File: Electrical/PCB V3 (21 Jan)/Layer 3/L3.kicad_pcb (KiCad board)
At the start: 2 copper layers, 129.9 x 110 mm, 28 parts, among them J1 Conn_01x06, J2 Conn_02x04_Odd_Even, J3 Conn_01x06, J4 Conn_01x06, J5 Conn_01x06, U2 113991054, U3 4754

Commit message: deleted some l3 stuff to clear up folders, open and closed l3
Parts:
- J2: value Conn_02x04_Odd_Even -> Conn_02x08_Odd_Even
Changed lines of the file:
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@@
 			)
 		)
-		(property "Value" "Conn_02x04_Odd_Even"
+		(property "Value" "Conn_02x08_Odd_Even"
 			(at 8.75 -3.4 90)
 			(layer "B.Fab")

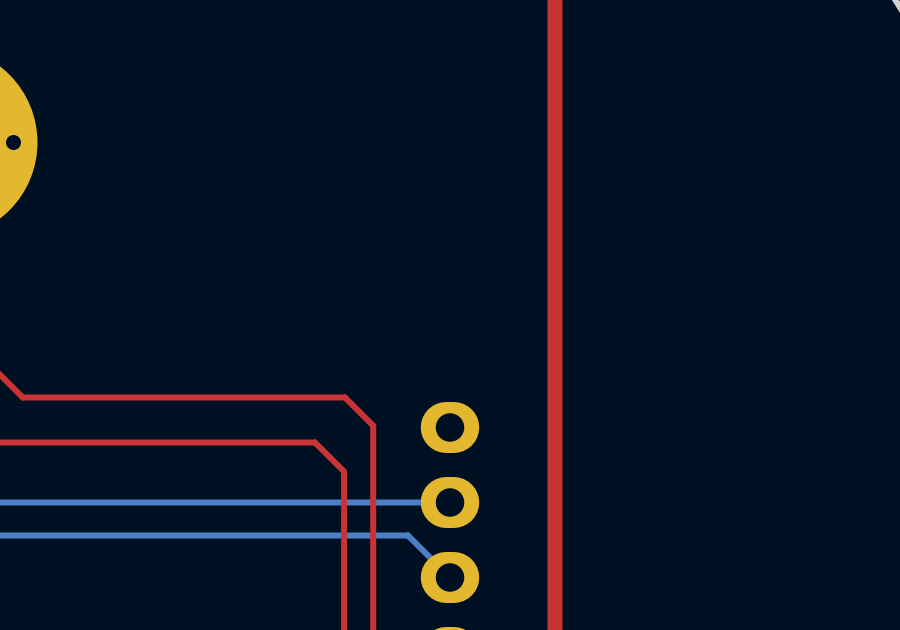
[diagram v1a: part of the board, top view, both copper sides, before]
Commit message: fixed l2 caps positon, export new l2 step. fixed l3 jst from eh to xh, realised need to flip l2 jst
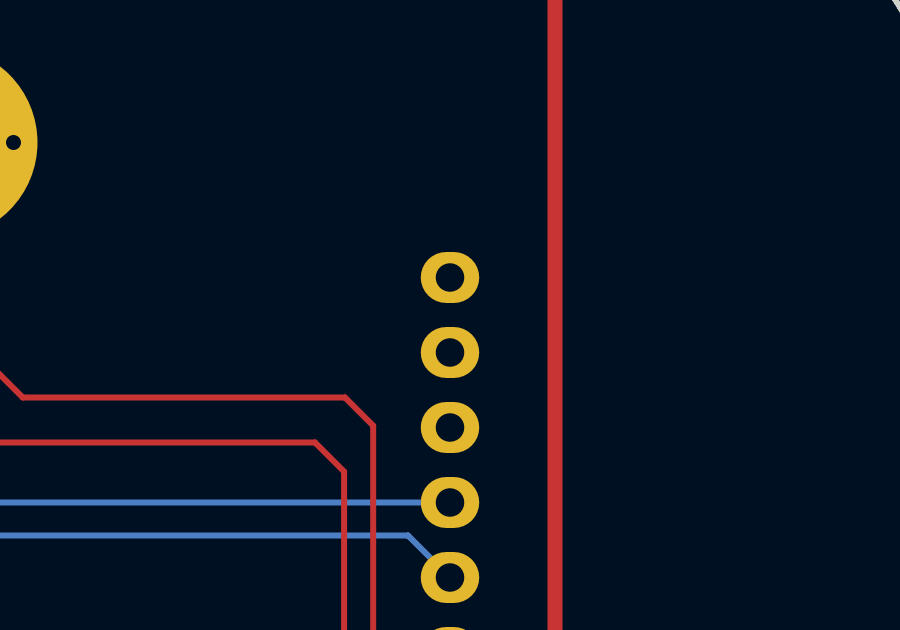
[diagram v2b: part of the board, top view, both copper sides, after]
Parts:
- J2: footprint Connector_JST:JST_EH_B8B-EH-A_1x08_P2.50mm_Vertical -> Connector_JST:JST_XH_B10B-XH-A_1x10_P2.50mm_Vertical
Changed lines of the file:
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@@
 			(at 0 15.03 0)
 			(layer "F.Fab")
+			(hide yes)
 			(effects
 				(font
@@
 			(at 0 15.03 90)
 			(layer "F.Fab")
+			(hide yes)
 			(effects
 				(font
@@
 			(at 0 15.03 90)
 			(layer "F.Fab")
+			(hide yes)
 			(effects
 				(font
@@
 		)
 		(property "Value" "Conn_01x06"
-			(at 0 15.03 0)
+			(at -0.75 -2.400001 0)
 			(layer "F.Fab")
+			(hide yes)
 			(effects
 				(font
@@
 		)
 	)
-	(footprint "Connector_JST:JST_EH_B8B-EH-A_1x08_P2.50mm_Vertical"
+	(footprint "Connector_JST:JST_XH_B10B-XH-A_1x10_P2.50mm_Vertical"
 		(layer "B.Cu")
 		(at 253.740001 84.530001 90)
-		(descr "JST EH series connector, B8B-EH-A (http://www.jst-mfg.com/product/pdf/eng/eEH.pdf), generated with kicad-footprint-generator")
-		(tags "connector JST EH vertical")
+		(descr "JST XH series connector, B10B-XH-A (http://www.jst-mfg.com/product/pdf/eng/eXH.pdf), generated with kicad-footprint-generator")
+		(tags "connector JST XH side entry")
 		(property "Reference" "J2"
-			(at 8.75 2.8 90)
+			(at 11.25 3.55 -90)
 			(layer "B.SilkS")
-			(hide yes)
 			(effects
 				(font
@@
 		)
 		(property "Value" "Conn_02x08_Odd_Even"
-			(at 8.75 -3.4 90)
+			(at 11.25 -4.6 -90)
 			(layer "B.Fab")
-			(hide yes)
 			(effects
 				(font
@@
 			)
 		)
-		(property "Footprint" "Connector_JST:JST_EH_B8B-EH-A_1x08_P2.50mm_Vertical"
+		(property "Footprint" "Connector_JST:JST_XH_B10B-XH-A_1x10_P2.50mm_Vertical"
 			(at 0 0 -90)
 			(unlocked yes)
@@
 		(attr through_hole)
 		(fp_line
-			(start -0.41 -2.61)
-			(end -2.91 -2.61)
+			(start 25.06 -3.51)
+			(end -2.56 -3.51)
+			(stroke
+				(width 0.12)
+				(type solid)
+			)
+			(layer "B.SilkS")
+		)
+		(fp_line
+			(start -2.56 -3.51)
+			(end -2.56 2.46)
+			(stroke
+				(width 0.12)
+				(type solid)
+			)
+			(layer "B.SilkS")
+		)
+		(fp_line
+			(start 24.3 -2.75)
+			(end 24.3 0.2)
+			(stroke
+				(width 0.12)
+				(type solid)
+			)
+			(layer "B.SilkS")
+		)
+		(fp_line
+			(start 11.25 -2.75)
+			(end 24.3 -2.75)
+			(stroke
+				(width 0.12)
+				(type solid)
+			)
+			(layer "B.SilkS")
+		)
+		(fp_line
+			(start 11.25 -2.75)
+			(end -1.8 -2.75)
+			(stroke
+				(width 0.12)
+				(type solid)
+			)
+			(layer "B.SilkS")
+		)
+		(fp_line
+			(start -1.8 -2.75)
+			(end -1.8 0.2)
+			(stroke
+				(width 0.12)
+				(type solid)
+			)
+			(layer "B.SilkS")
+		)
+		(fp_line
+			(start 24.3 0.2)
+			(end 25.05 0.2)
+			(stroke
+				(width 0.12)
+				(type solid)
+			)
+			(layer "B.SilkS")
+		)
+		(fp_line
+			(start -1.8 0.2)
+			(end -2.55 0.2)
 			(stroke
 				(width 0.12)
@@
 		)
 		(fp_line
-			(start -2.91 -2.61)
-			(end -2.91 -0.11)
+			(start -2.85 1.5)
+			(end -2.85 2.75)
 			(stroke
 				(width 0.12)
@@
 		)
 		(fp_line
-			(start 20.11 -2.31)
-			(end -2.61 -2.31)
+			(start 25.05 1.7)
+			(end 23.25 1.7)
 			(stroke
 				(width 0.12)
@@
 		)
 		(fp_line
-			(start 19.11 -2.31)
-			(end 19.11 -0.81)
+			(start 23.25 1.7)
+			(end 23.25 2.45)
 			(stroke
 				(width 0.12)
@@
 		)
 		(fp_line
-			(start -1.61 -2.31)
-			(end -1.61 -0.81)
+			(start 21.75 1.7)
+			(end 0.75 1.7)
 			(stroke
 				(width 0.12)
@@
 		)
 		(fp_line
-			(start -2.61 -2.31)
-			(end -2.61 1.71)
+			(start 0.75 1.7)
+			(end 0.75 2.45)
 			(stroke
 				(width 0.12)
@@
 		)
 		(fp_line
-			(start 19.11 -0.81)
-			(end 20.11 -0.81)
+			(start -0.75 1.7)
+			(end -2.55 1.7)
 			(stroke
 				(width 0.12)
@@
 		)
 		(fp_line
-			(start -1.61 -0.81)
-			(end -2.61 -0.81)
+			(start -2.55 1.7)
+			(end -2.55 2.45)
 			(stroke
 				(width 0.12)
@@
 		)
 		(fp_line
-			(start 20.11 0)
-			(end 19.61 0)
+			(start 25.05 2.45)
+			(end 25.05 1.7)
 			(stroke
 				(width 0.12)
@@
 		)
 		(fp_line
-			(start 19.61 0)
-			(end 19.61 1.21)
+			(start 23.25 2.45)
+			(end 25.05 2.45)
 			(stroke
 				(width 0.12)
@@
 		)
 		(fp_line
-			(start -2.11 0)
-			(end -2.61 0)
+			(start 21.75 2.45)
+			(end 21.75 1.7)
 			(stroke
 				(width 0.12)
@@
 		)
 		(fp_line
-			(start 19.61 1.21)
-			(end -2.11 1.21)
+			(start 0.75 2.45)
+			(end 21.75 2.45)
 			(stroke
 				(width 0.12)
@@
 		)
 		(fp_line
-			(start -2.11 1.21)
-			(end -2.11 0)
+			(start -0.75 2.45)
+			(end -0.75 1.7)
 			(stroke
 				(width 0.12)
@@
 		)
 		(fp_line
-			(start 20.11 1.71)
-			(end 20.11 -2.31)
+			(start -2.55 2.45)
+			(end -0.75 2.45)
 			(stroke
 				(width 0.12)
@@
 		)
 		(fp_line
-			(start -2.61 1.71)
-			(end 20.11 1.71)
+			(start 25.06 2.46)
+			(end 25.06 -3.51)
 			(stroke
 				(width 0.12)
@@
 		)
 		(fp_line
-			(start 20.5 -2.7)
-			(end -3 -2.7)
+			(start -2.56 2.46)
+			(end 25.06 2.46)
+			(stroke
+				(width 0.12)
+				(type solid)
+			)
+			(layer "B.SilkS")
+		)
+		(fp_line
+			(start -2.85 2.75)
+			(end -1.6 2.75)
+			(stroke
+				(width 0.12)
+				(type solid)
+			)
+			(layer "B.SilkS")
+		)
+		(fp_line
+			(start 25.45 -3.9)
+			(end -2.95 -3.9)
 			(stroke
 				(width 0.05)
@@
 		)
 		(fp_line
-			(start -3 -2.7)
-			(end -3 2.1)
+			(start -2.95 -3.9)
+			(end -2.95 2.85)
 			(stroke
 				(width 0.05)
@@
 		)
 		(fp_line
-			(start 20.5 2.1)
-			(end 20.5 -2.7)
+			(start 25.45 2.85)
+			(end 25.45 -3.9)
 			(stroke
 				(width 0.05)
@@
 		)
 		(fp_line
-			(start -3 2.1)
-			(end 20.5 2.1)
+			(start -2.95 2.85)
+			(end 25.45 2.85)
 			(stroke
 				(width 0.05)
@@
 		)
 		(fp_line
-			(start -0.41 -2.61)
-			(end -2.91 -2.61)
+			(start 24.95 -3.4)
+			(end -2.45 -3.4)
 			(stroke
 				(width 0.1)
@@
 		)
 		(fp_line
-			(start -2.91 -2.61)
-			(end -2.91 -0.11)
+			(start -2.45 -3.4)
+			(end -2.45 2.35)
 			(stroke
 				(width 0.1)
@@
 		)
 		(fp_line
-			(start 20 -2.2)
-			(end -2.5 -2.2)
+			(start 0 1.35)
+			(end -0.625 2.35)
 			(stroke
 				(width 0.1)
@@
 		)
 		(fp_line
-			(start -2.5 -2.2)
-			(end -2.5 1.6)
+			(start 24.95 2.35)
+			(end 24.95 -3.4)
 			(stroke
 				(width 0.1)
@@
 		)
 		(fp_line
-			(start 20 1.6)
-			(end 20 -2.2)
+			(start 0.625 2.35)
+			(end 0 1.35)
 			(stroke
 				(width 0.1)
@@
 		)
 		(fp_line
-			(start -2.5 1.6)
-			(end 20 1.6)
+			(start -2.45 2.35)
+			(end 24.95 2.35)
 			(stroke
 				(width 0.1)
@@
 			(layer "B.Fab")
 		)
+		(fp_text user "${REFERENCE}"
+			(at 11.25 -2.7 -90)
+			(layer "B.Fab")
+			(effects
+				(font
+					(size 1 1)
+					(thickness 0.15)
+				)
+				(justify mirror)
+			)
+		)
 		(pad "1" thru_hole roundrect
 			(at 0 0 90)
@@
 			(pintype "passive")
 		)
-		(model "${KICAD8_3DMODEL_DIR}/Connector_JST.3dshapes/JST_EH_B8B-EH-A_1x08_P2.50mm_Vertical.wrl"
+		(pad "9" thru_hole oval
+			(at 20 0 90)
+			(size 1.7 1.95)
+			(drill 0.95)
+			(layers "*.Cu" "*.Mask")
+			(remove_unused_layers no)
+		)
+		(pad "10" thru_hole oval
+			(at 22.5 0 90)
+			(size 1.7 1.95)
+			(drill 0.95)
+			(layers "*.Cu" "*.Mask")
+			(remove_unused_layers no)
+		)
+		(model "${KICAD8_3DMODEL_DIR}/Connector_JST.3dshapes/JST_XH_B10B-XH-A_1x10_P2.50mm_Vertical.wrl"
 			(offset
 				(xyz 0 0 0)

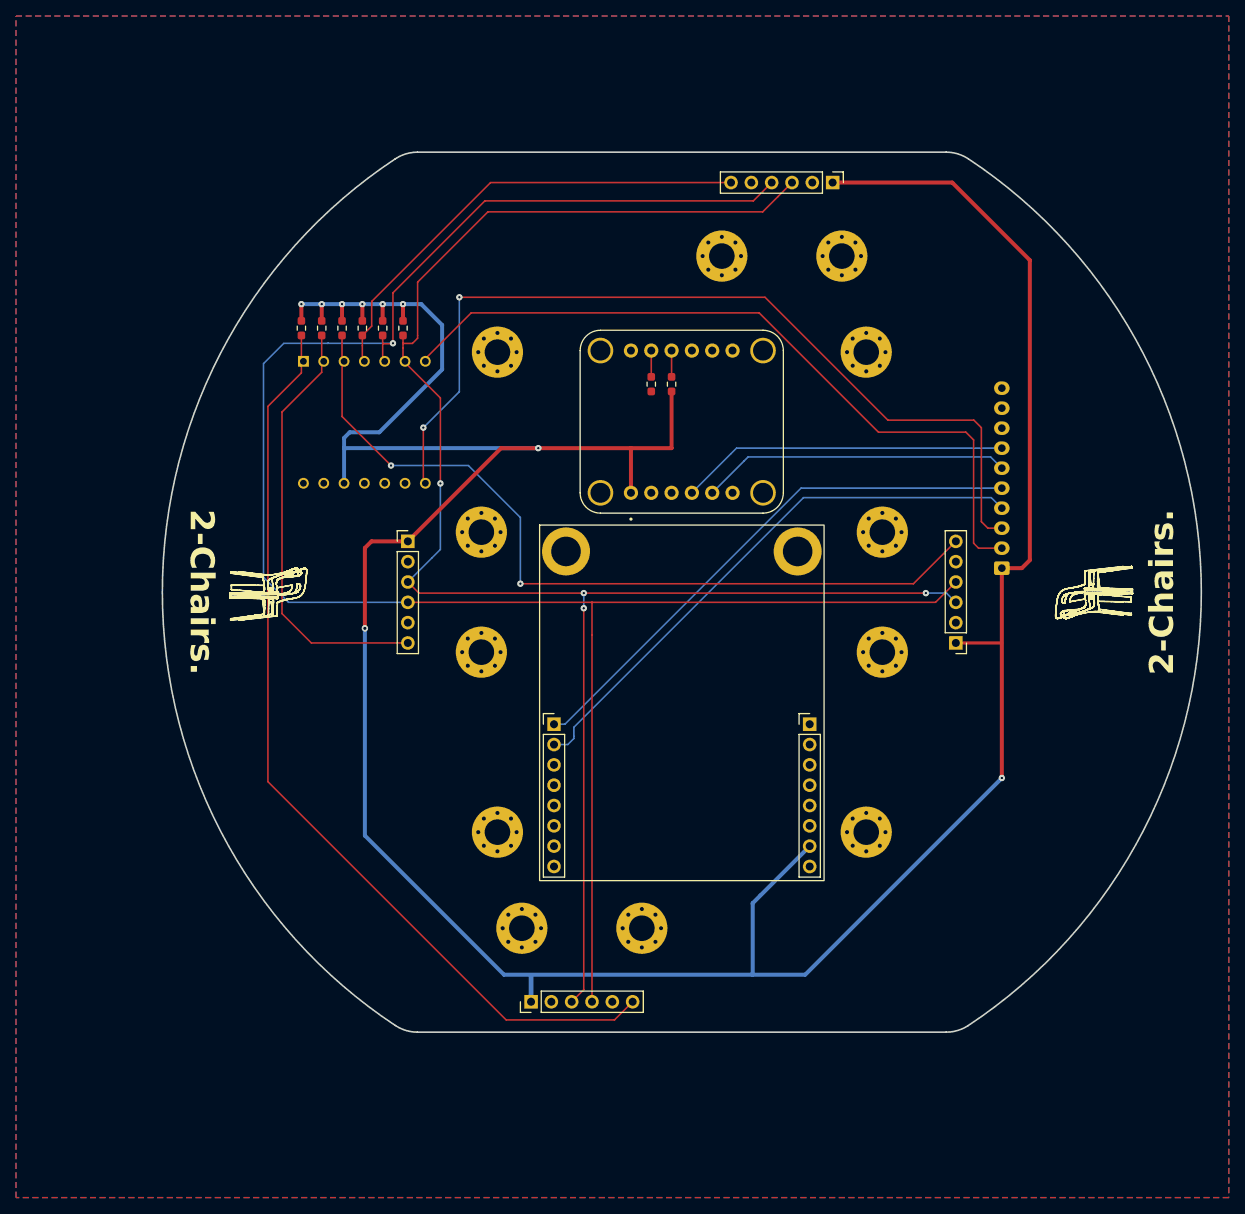
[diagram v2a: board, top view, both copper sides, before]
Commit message: fixed l3 edge cut in 5min what an accomplishment
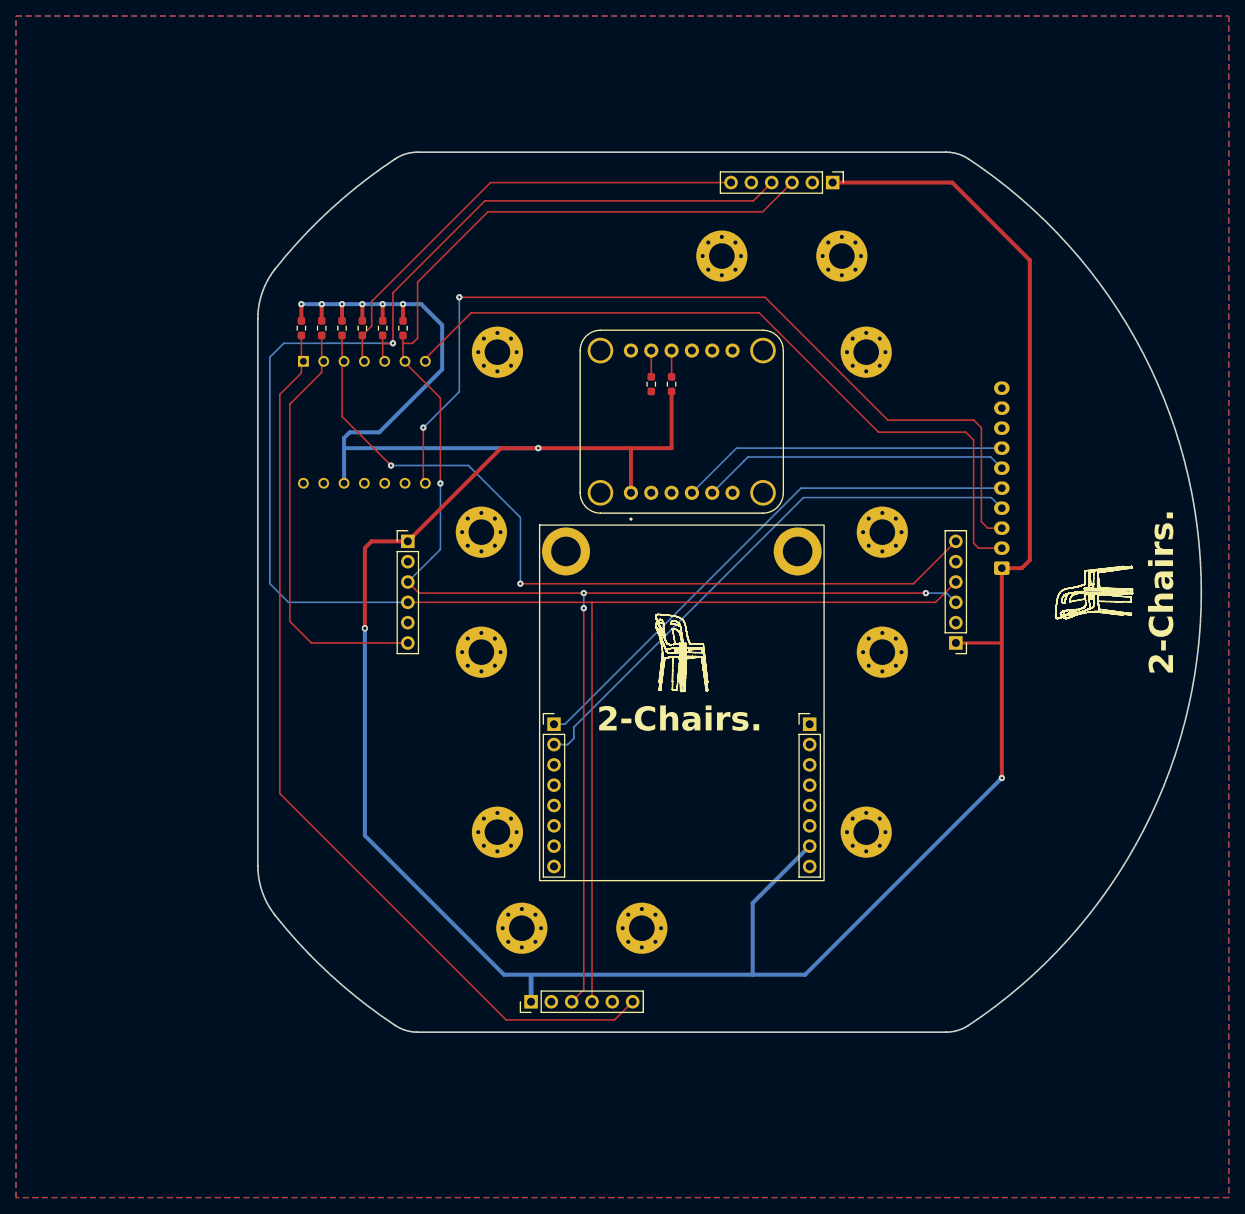
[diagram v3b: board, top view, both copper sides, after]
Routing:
- net /TOF1 XSHUT: track 116.4 -> 115.1 mm
- net /TOF2 XSHUT: track 54.1 -> 53.3 mm
- net /SDA: track 246.6 -> 245.9 mm
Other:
- board size 129.9 x 110 mm -> 117.9 x 110 mm

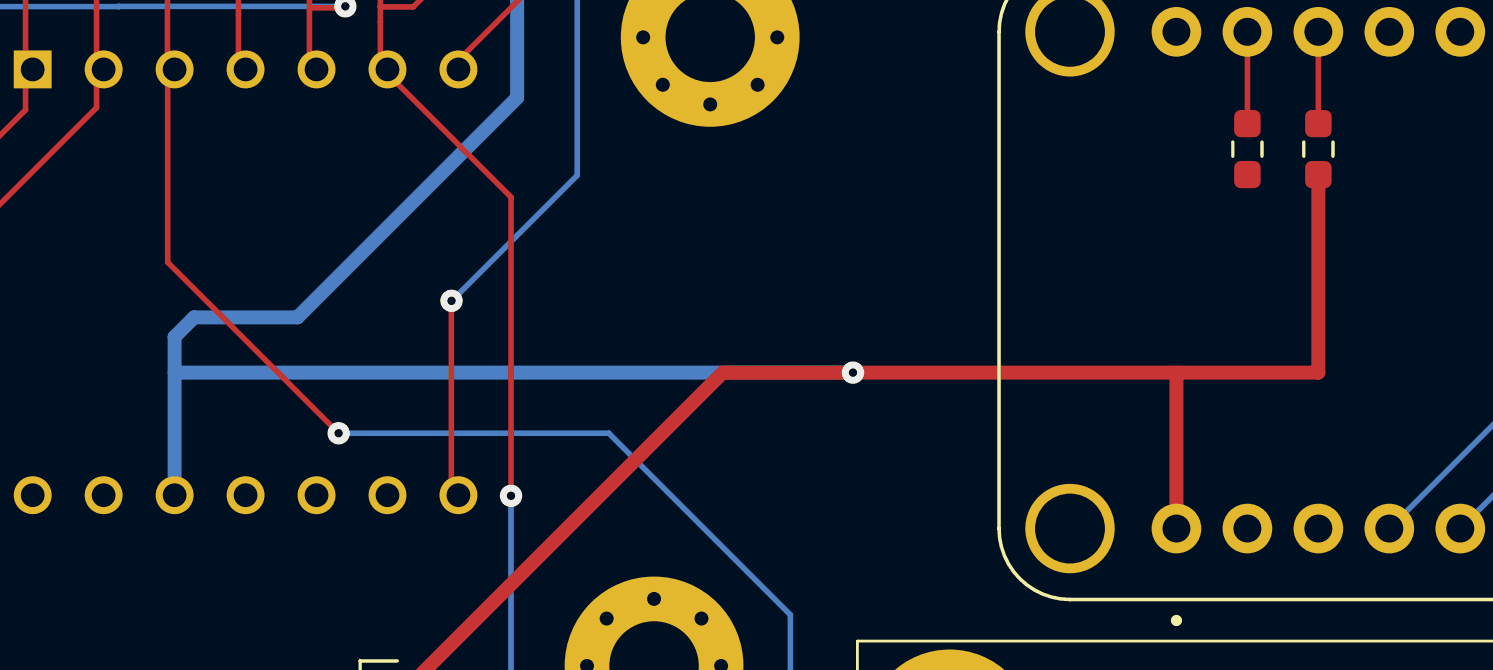
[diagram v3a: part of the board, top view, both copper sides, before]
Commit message: shopuld have fixed l1 and l3 based on kian wu comments
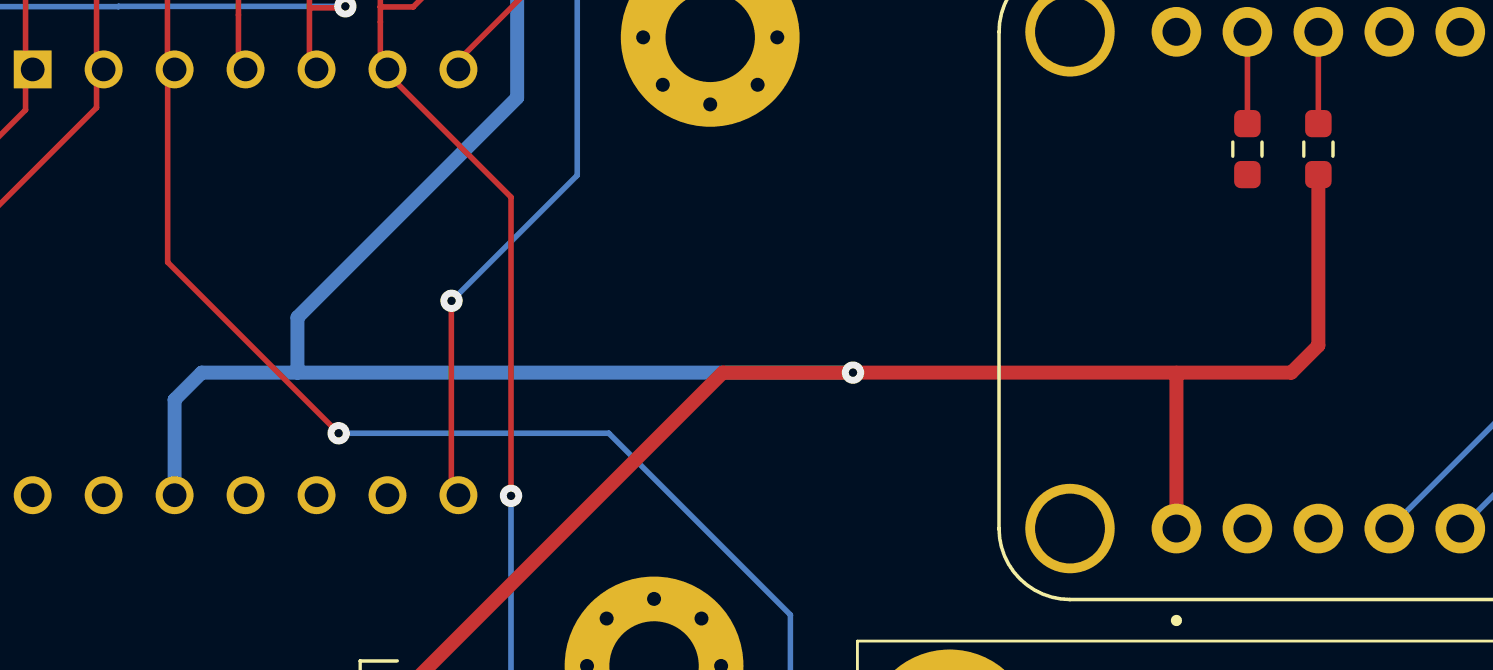
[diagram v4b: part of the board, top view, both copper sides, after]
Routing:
- net +3V3: track 396.0 -> 390.8 mm
